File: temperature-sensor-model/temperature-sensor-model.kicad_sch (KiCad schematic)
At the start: 11 parts, among them J1 Conn_01x01_Female, J2 Conn_01x01_Female, Q1 2N2219

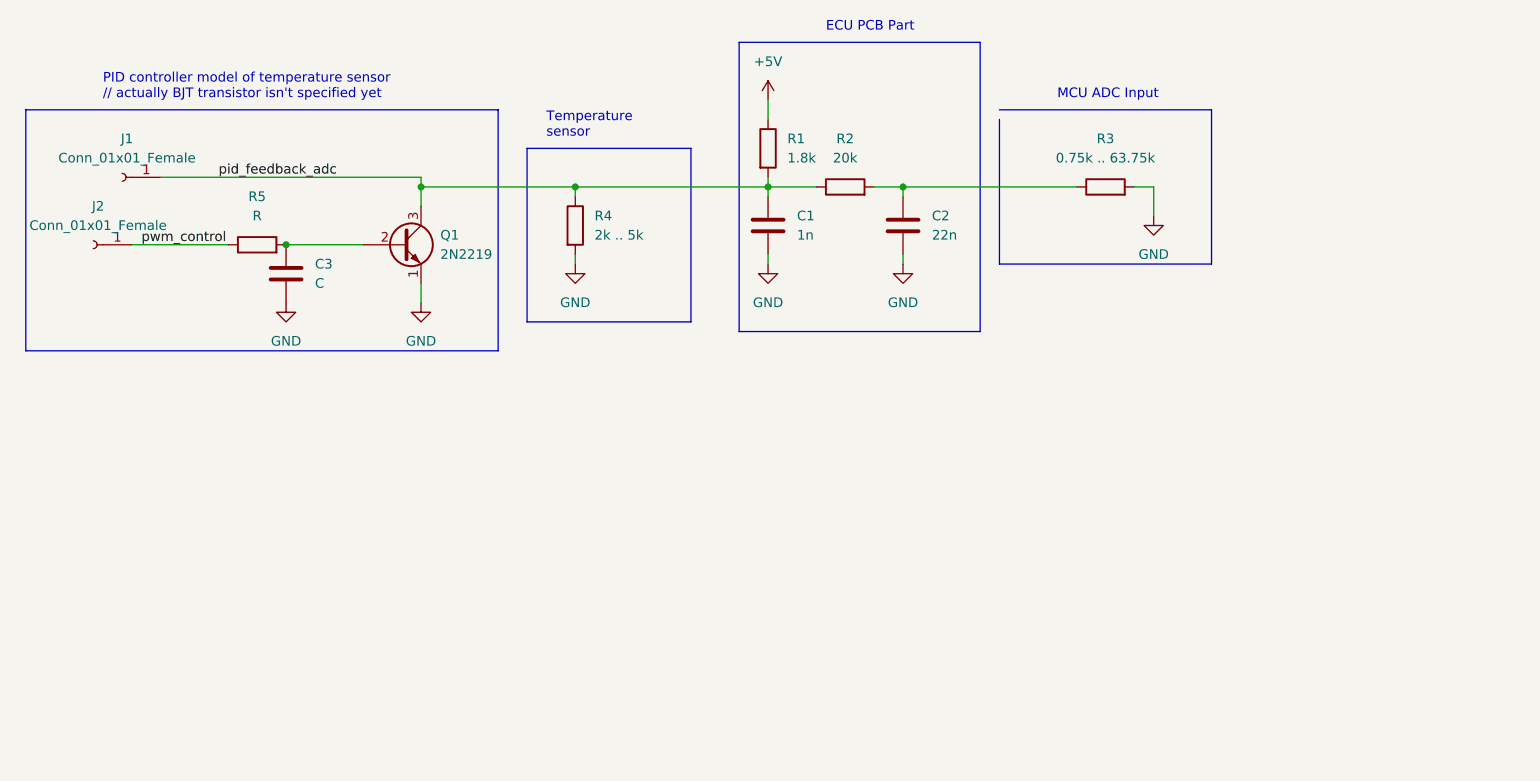
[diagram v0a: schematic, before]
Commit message: [T sensor model] Update temp sensor model
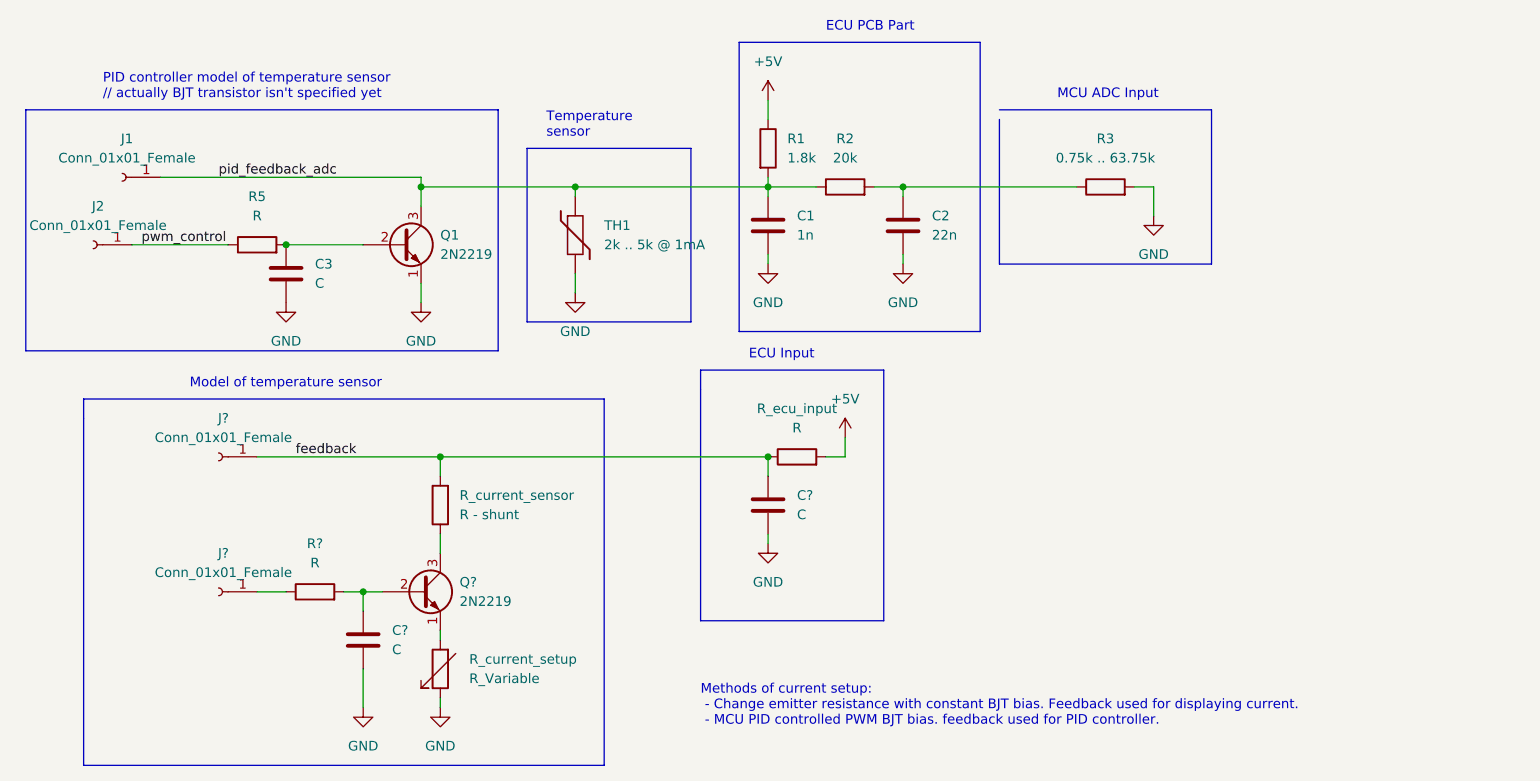
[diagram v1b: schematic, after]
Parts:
- removed R4: 2k .. 5k, symbol Device:R
- added C? (x2): C, symbol Device:C
- added J? (x2): Conn_01x01_Female, symbol Connector:Conn_01x01_Female
- added Q?: 2N2219, Package_TO_SOT_THT:TO-39-3, symbol Transistor_BJT:2N2219
- added R?, R_ecu_input: R, symbol Device:R
- added R_current_sensor: R - shunt, symbol Device:R
- added R_current_setup: R_Variable, symbol Device:R_Variable
- added TH1: 2k .. 5k @ 1mA, symbol Device:Thermistor
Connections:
- net +5V: now also R_ecu_input.2
- net GND: now also C?.2, C?.2, R_current_setup.1, TH1.2
- net pid_feedback_adc: now also TH1.1
- new net: J?.1 (Pin_1), R?.1
- new net: C?.1, Q?.2 (B), R?.2
- new net: Q?.1 (E), R_current_setup.2
- new net: Q?.3 (C), R_current_sensor.1
- new net feedback: C?.1, J?.1 (Pin_1), R_current_sensor.2, R_ecu_input.1
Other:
- note added: "ECU Input"
- note added: "Methods of current setup: - Change emitter resistance with constant BJT bias. Feedback used for displaying current. - MCU PID controlled PWM BJT bias. feedback used for PID controller."
- note added: "Model of temperature sensor"
